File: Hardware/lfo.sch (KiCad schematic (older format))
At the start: 0 parts

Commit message: add bill of materials spreadsheet and begin to populate with values
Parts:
- added C?: 33nF, symbol C_Small
- added C? (x2): 220uF, symbol CP1_Small
- added Q?: 2N3904, TO_SOT_Packages_THT:TO-92_Molded_Narrow, symbol 2N3904
- added R? (x2): 10k, symbol R
- added RV? (x2): 10k, symbol POT
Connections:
- new net: Q?.1 (E), R?.1, RV?.3
- new net: C?.1, Q?.3 (C), R?.2
- new net: C?.1, C?.2, RV?.1, RV?.2
- new net: C?.2, RV?.1
- new net +15V: R?.1
- new net GND: R?.2, RV?.3
- new net bias: C?.1, Q?.2 (B)
- new net lfo1: RV?.2
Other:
- note added: "Double check conrner \nfrequency of DC blocking \ncaps."
- note added: "lfo1 mod level"
- note added: "lfo_1 phase"
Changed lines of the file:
@@
 Comment4 ""
 $EndDescr
+$Comp
+L 2N3904 Q?
+U 1 1 5C367DF2
+P 5150 1650
+F 0 "Q?" H 5350 1725 50  0000 L CNN
+F 1 "2N3904" H 5350 1650 50  0000 L CNN
+F 2 "TO_SOT_Packages_THT:TO-92_Molded_Narrow" H 5350 1575 50  0001 L CIN
+F 3 "" H 5150 1650 50  0001 L CNN
+	1    5150 1650
+	1    0    0    -1
+$EndComp
+Text Label 4750 1500 0    60   ~ 0
+bias
+$Comp
+L R R?
+U 1 1 5C367F46
+P 5250 1150
+F 0 "R?" V 5330 1150 50  0000 C CNN
+F 1 "10k" V 5250 1150 50  0000 C CNN
+F 2 "" V 5180 1150 50  0001 C CNN
+F 3 "" H 5250 1150 50  0001 C CNN
+	1    5250 1150
+	1    0    0    -1
+$EndComp
+$Comp
+L R R?
+U 1 1 5C367FA3
+P 5250 2150
+F 0 "R?" V 5330 2150 50  0000 C CNN
+F 1 "10k" V 5250 2150 50  0000 C CNN
+F 2 "" V 5180 2150 50  0001 C CNN
+F 3 "" H 5250 2150 50  0001 C CNN
+	1    5250 2150
+	1    0    0    -1
+$EndComp
+$Comp
+L GND #PWR?
+U 1 1 5C367FDF
+P 5250 2350
+F 0 "#PWR?" H 5250 2100 50  0001 C CNN
+F 1 "GND" H 5250 2200 50  0000 C CNN
+F 2 "" H 5250 2350 50  0001 C CNN
+F 3 "" H 5250 2350 50  0001 C CNN
+	1    5250 2350
+	1    0    0    -1
+$EndComp
+$Comp
+L +15V #PWR?
+U 1 1 5C368017
+P 5250 950
+F 0 "#PWR?" H 5250 800 50  0001 C CNN
+F 1 "+15V" H 5250 1090 50  0000 C CNN
+F 2 "" H 5250 950 50  0001 C CNN
+F 3 "" H 5250 950 50  0001 C CNN
+	1    5250 950
+	1    0    0    -1
+$EndComp
+$Comp
+L C_Small C?
+U 1 1 5C368040
+P 5700 1500
+F 0 "C?" H 5710 1570 50  0000 L CNN
+F 1 "33nF" H 5710 1420 50  0000 L CNN
+F 2 "" H 5700 1500 50  0001 C CNN
+F 3 "" H 5700 1500 50  0001 C CNN
+	1    5700 1500
+	1    0    0    -1
+$EndComp
+$Comp
+L POT RV?
+U 1 1 5C368098
+P 5700 1800
+F 0 "RV?" V 5525 1800 50  0000 C CNN
+F 1 "10k" V 5600 1800 50  0000 C CNN
+F 2 "" H 5700 1800 50  0001 C CNN
+F 3 "" H 5700 1800 50  0001 C CNN
+	1    5700 1800
+	1    0    0    -1
+$EndComp
+Wire Wire Line
+	4600 1650 4950 1650
+Wire Wire Line
+	5250 2350 5250 2300
+Wire Wire Line
+	5250 1850 5250 2000
+Wire Wire Line
+	5250 1300 5250 1450
+Wire Wire Line
+	5250 950  5250 1000
+Wire Wire Line
+	5700 1400 5700 1350
+Wire Wire Line
+	5700 1350 5250 1350
+Connection ~ 5250 1350
+Wire Wire Line
+	5700 1650 5700 1600
+Wire Wire Line
+	5850 1800 5850 1600
+Wire Wire Line
+	5700 1600 6250 1600
+Wire Wire Line
+	5700 1950 5250 1950
+Connection ~ 5250 1950
+Connection ~ 5850 1600
+Wire Wire Line
+	4750 1500 4750 1650
+Connection ~ 4750 1650
+$Comp
+L CP1_Small C?
+U 1 1 5C36835D
+P 4500 1650
+F 0 "C?" H 4510 1720 50  0000 L CNN
+F 1 "220uF" H 4510 1570 50  0000 L CNN
+F 2 "" H 4500 1650 50  0001 C CNN
+F 3 "" H 4500 1650 50  0001 C CNN
+	1    4500 1650
+	0    1    1    0
+$EndComp
+$Comp
+L CP1_Small C?
+U 1 1 5C368390
+P 6350 1600
+F 0 "C?" H 6360 1670 50  0000 L CNN
+F 1 "220uF" H 6360 1520 50  0000 L CNN
+F 2 "" H 6350 1600 50  0001 C CNN
+F 3 "" H 6350 1600 50  0001 C CNN
+	1    6350 1600
+	0    -1   -1   0
+$EndComp
+Text Notes 6050 1400 0    60   ~ 0
+Double check conrner \nfrequency of DC blocking \ncaps.
+Text HLabel 7000 1900 2    60   Output ~ 0
+lfo1
+Text Notes 6300 1950 2    60   ~ 0
+lfo_1 phase
+$Comp
+L POT RV?
+U 1 1 5C36940A
+P 6700 1900
+F 0 "RV?" V 6525 1900 50  0000 C CNN
+F 1 "10k" V 6600 1900 50  0000 C CNN
+F 2 "" H 6700 1900 50  0001 C CNN
+F 3 "" H 6700 1900 50  0001 C CNN
+	1    6700 1900
+	1    0    0    -1
+$EndComp
+Wire Wire Line
+	7000 1900 6850 1900
+Wire Wire Line
+	6700 1750 6700 1600
+Wire Wire Line
+	6700 1600 6450 1600
+$Comp
+L GND #PWR?
+U 1 1 5C3694AC
+P 6700 2100
+F 0 "#PWR?" H 6700 1850 50  0001 C CNN
+F 1 "GND" H 6700 1950 50  0000 C CNN
+F 2 "" H 6700 2100 50  0001 C CNN
+F 3 "" H 6700 2100 50  0001 C CNN
+	1    6700 2100
+	1    0    0    -1
+$EndComp
+Wire Wire Line
+	6700 2100 6700 2050
+Text Notes 7450 2050 2    60   ~ 0
+lfo1 mod level
 $EndSCHEMATC

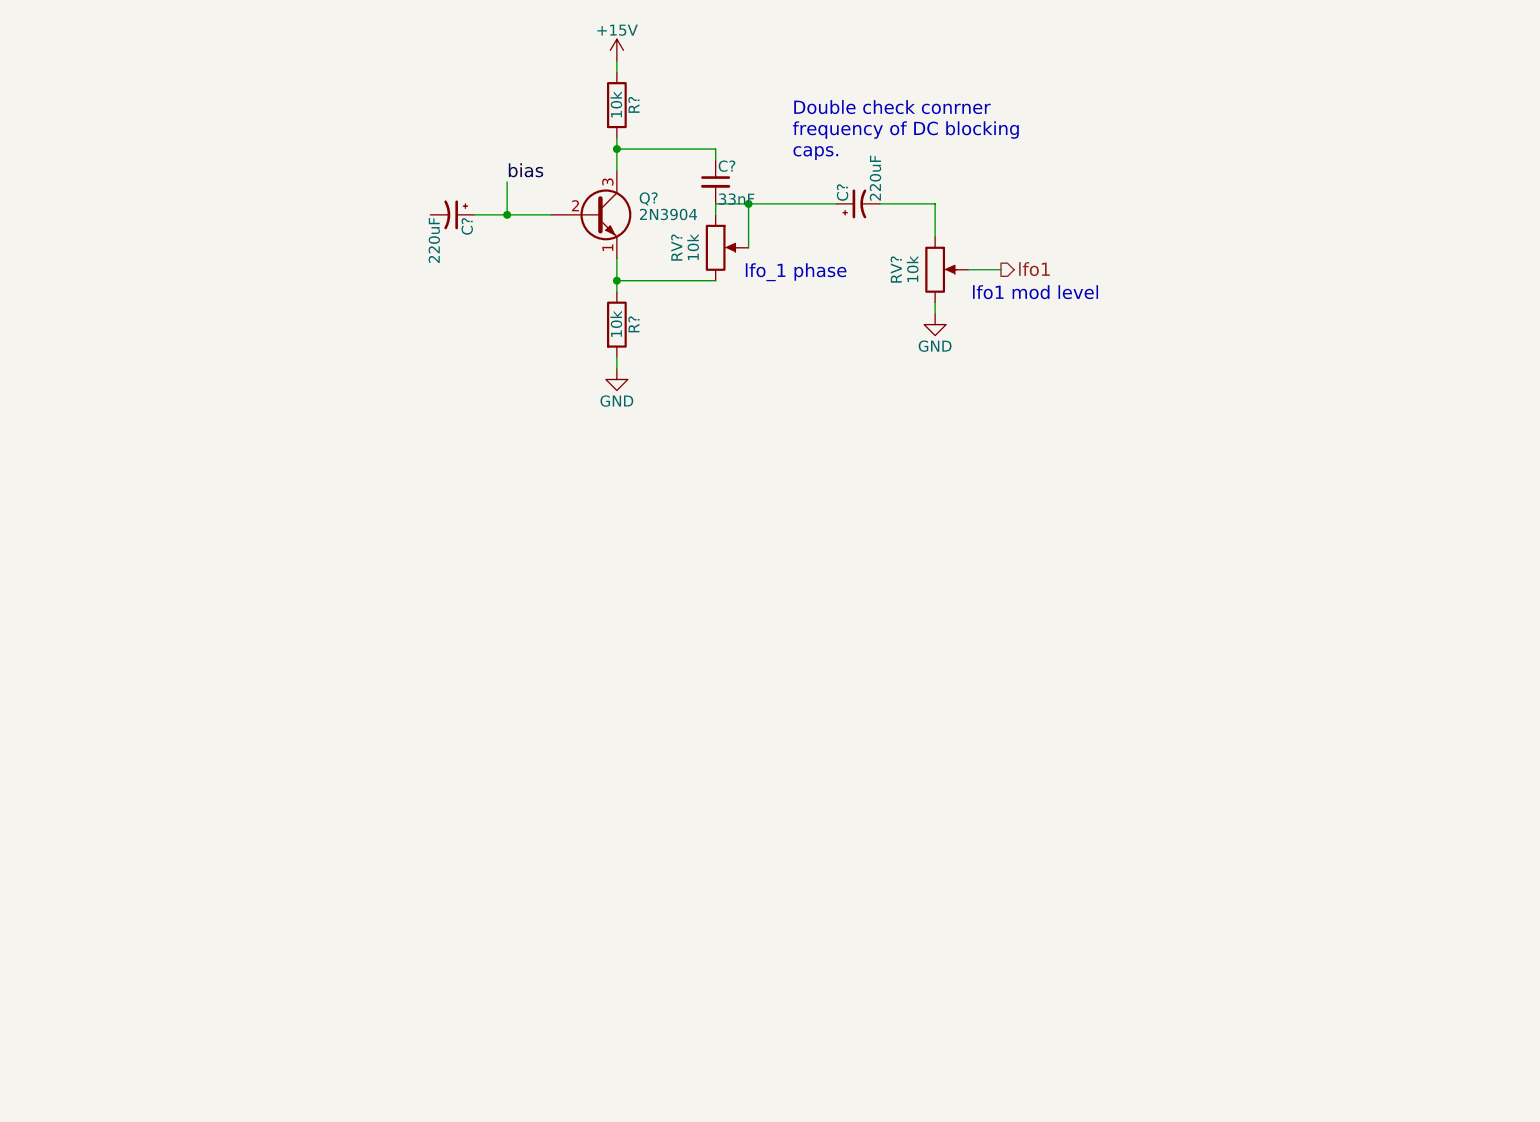
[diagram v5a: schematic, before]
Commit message: complete wiring of top level schematic hierarchical pages
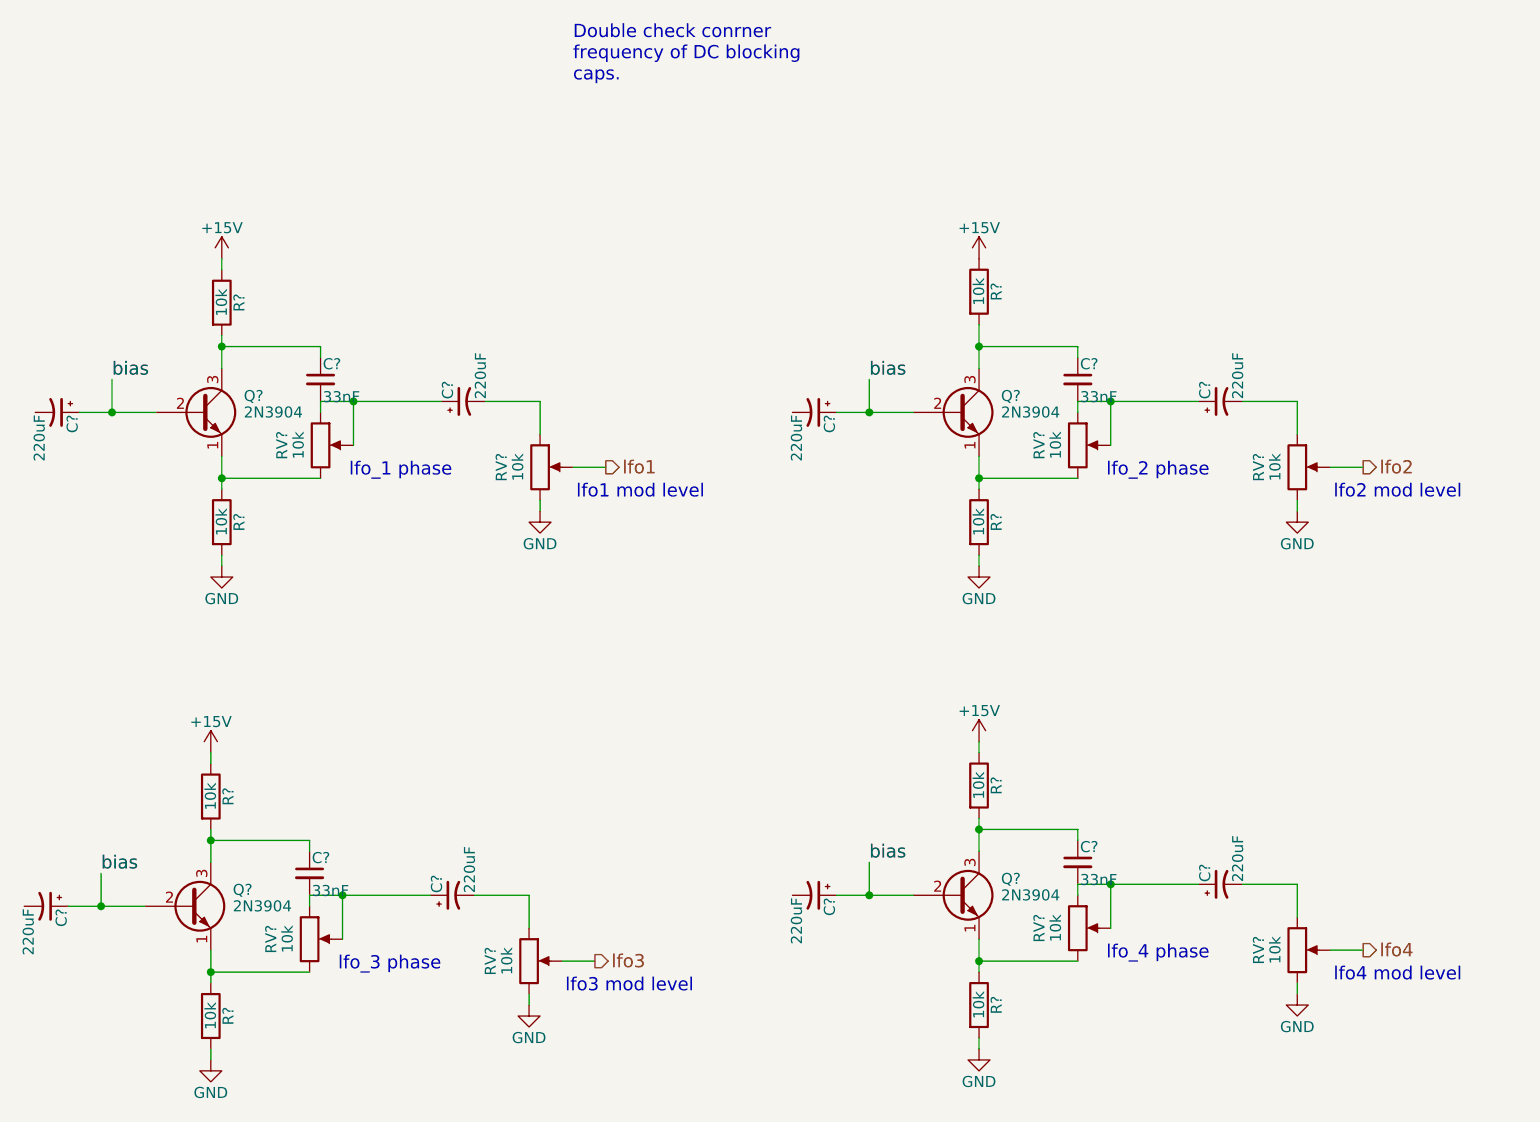
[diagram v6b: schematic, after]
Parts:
- added C? (x3): 33nF, symbol C_Small
- added C? (x6): 220uF, symbol CP1_Small
- added Q? (x3): 2N3904, TO_SOT_Packages_THT:TO-92_Molded_Narrow, symbol 2N3904
- added R? (x6): 10k, symbol R
- added RV? (x6): 10k, symbol POT
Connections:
- net +15V: now also R?.1, R?.1, R?.1
- net GND: now also R?.2, R?.2, R?.2, RV?.3, RV?.3, RV?.3
- net bias: now also C?.1, C?.1, C?.1, Q?.2 (B), Q?.2 (B), Q?.2 (B)
- new net: Q?.1 (E), R?.1, RV?.3 (x3)
- new net: C?.1, Q?.3 (C), R?.2 (x3)
- new net: C?.1, C?.2, RV?.1, RV?.2 (x3)
- new net: C?.2, RV?.1 (x3)
- new net lfo2: RV?.2
- new net lfo3: RV?.2
- new net lfo4: RV?.2
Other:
- note added: "lfo2 mod level"
- note added: "lfo3 mod level"
- note added: "lfo4 mod level"
- note added: "lfo_2 phase"
- note added: "lfo_3 phase"
- note added: "lfo_4 phase"
- moved on the sheet: C?, Q?, R?, RV?

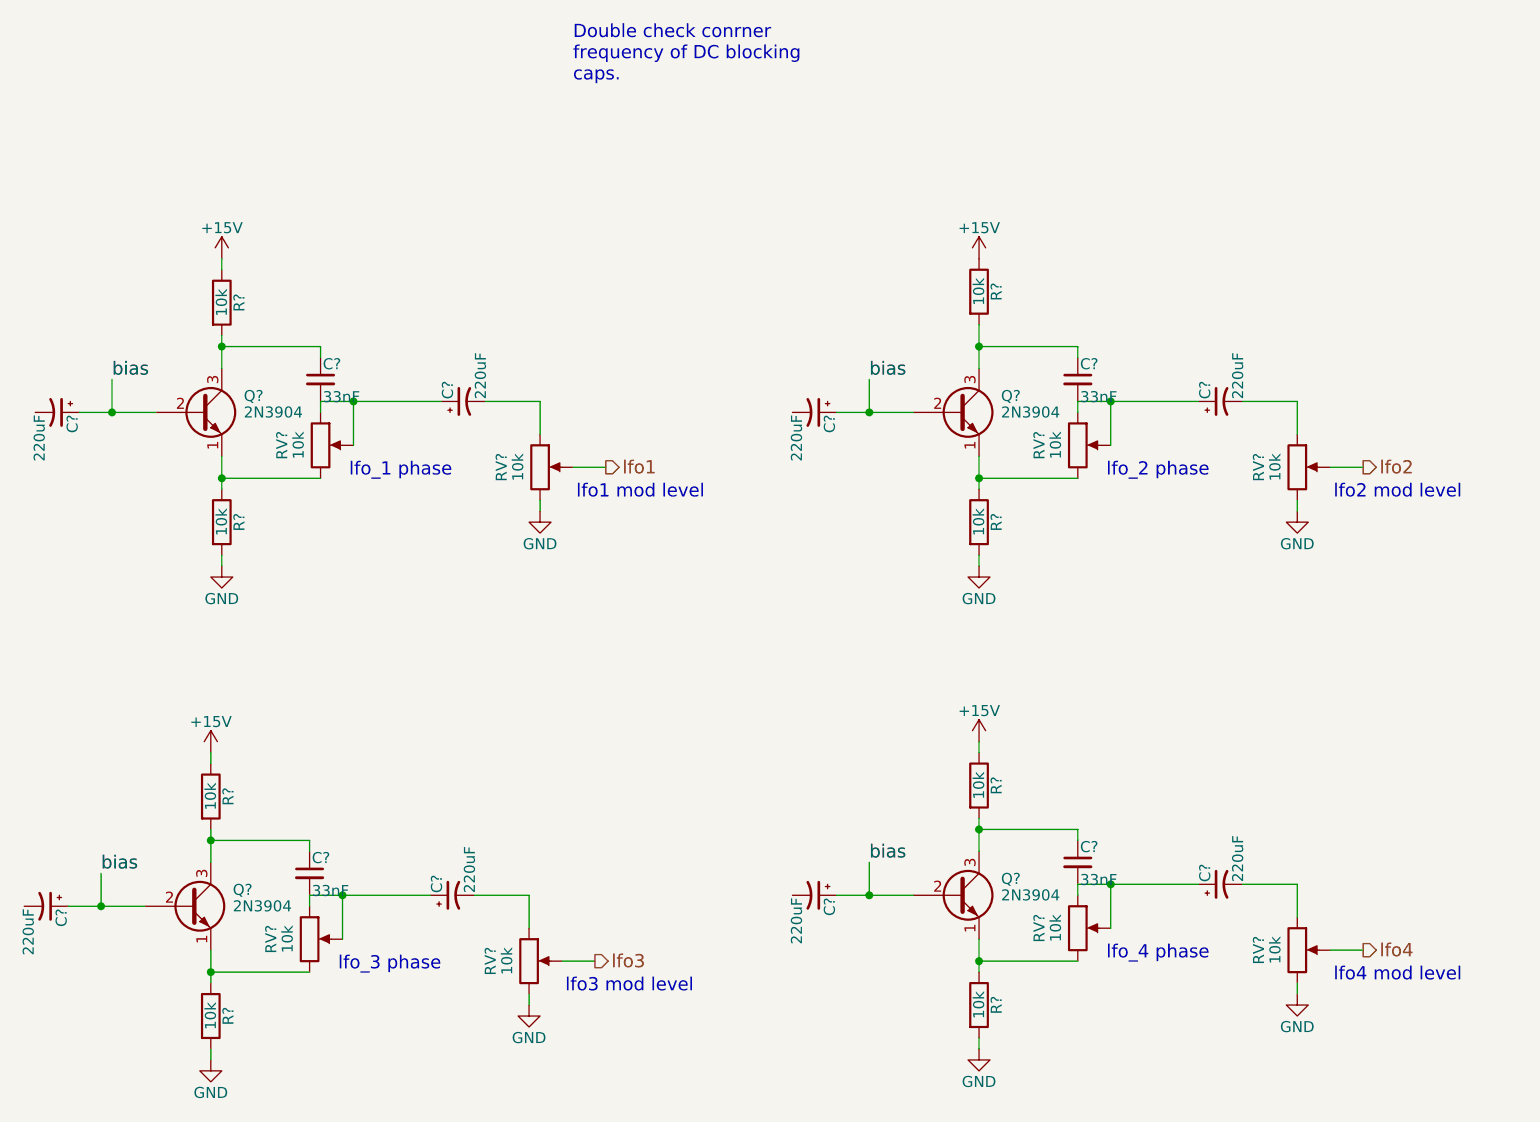
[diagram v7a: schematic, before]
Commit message: add power jack, 3.3V regulator, VREF divider
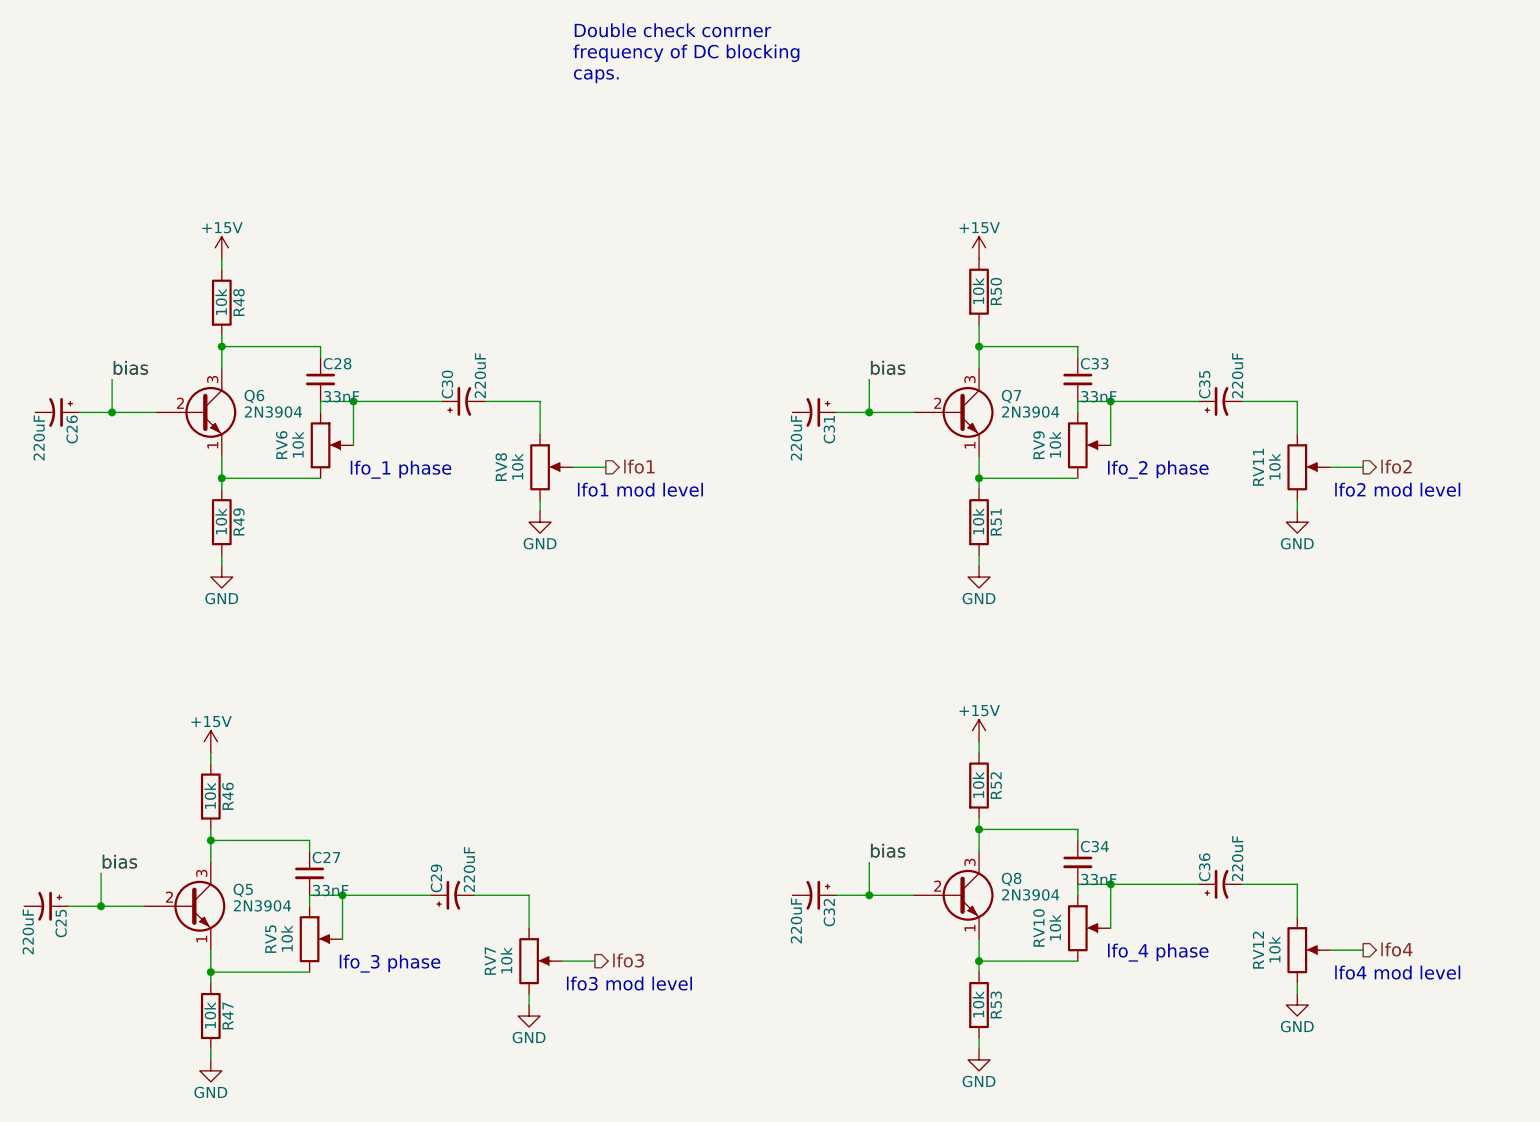
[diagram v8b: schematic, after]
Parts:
- gave numbers to parts that had none: 32
